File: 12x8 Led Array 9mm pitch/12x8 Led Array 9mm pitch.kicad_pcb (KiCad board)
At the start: 4 copper layers, 189 x 139.9 mm, 313 parts, among them J1 LED ch 1-24, J2 LED ch 25-48, J3 LED ch 49-72, J4 LED ch 73-96, J5 logic/analog, U1 CD74HC4067M96, U2 CD74HC4067M96, U3 CD74HC4067M96, U4 CD74HC4067M96, U5 CD74HC4067M96, U6 CD74HC4067M96

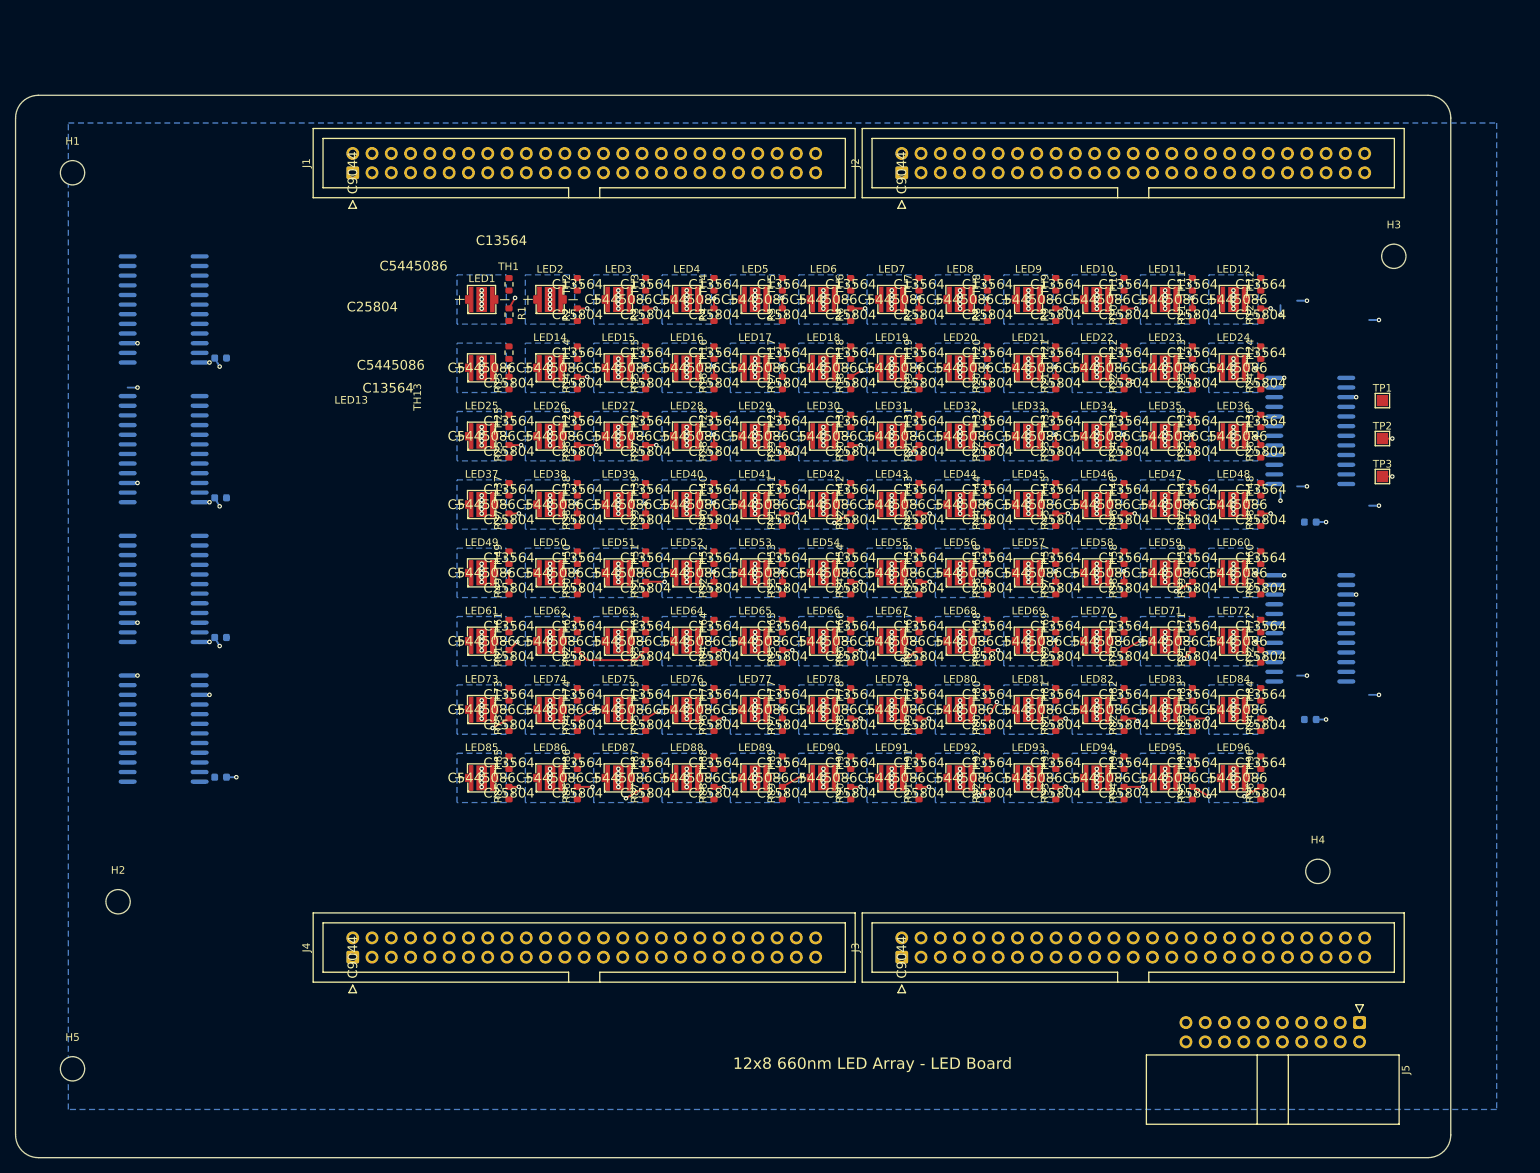
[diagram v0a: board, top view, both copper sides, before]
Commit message: 15mm keep-out from array for all support parts; J5 joins right mux pair
Co-Authored-By: Claude Fable 5 <noreply@anthropic.com>
Claude-Session: https://claude.ai/code/session_017oD54uh7Tvu54u9NPQNcZB
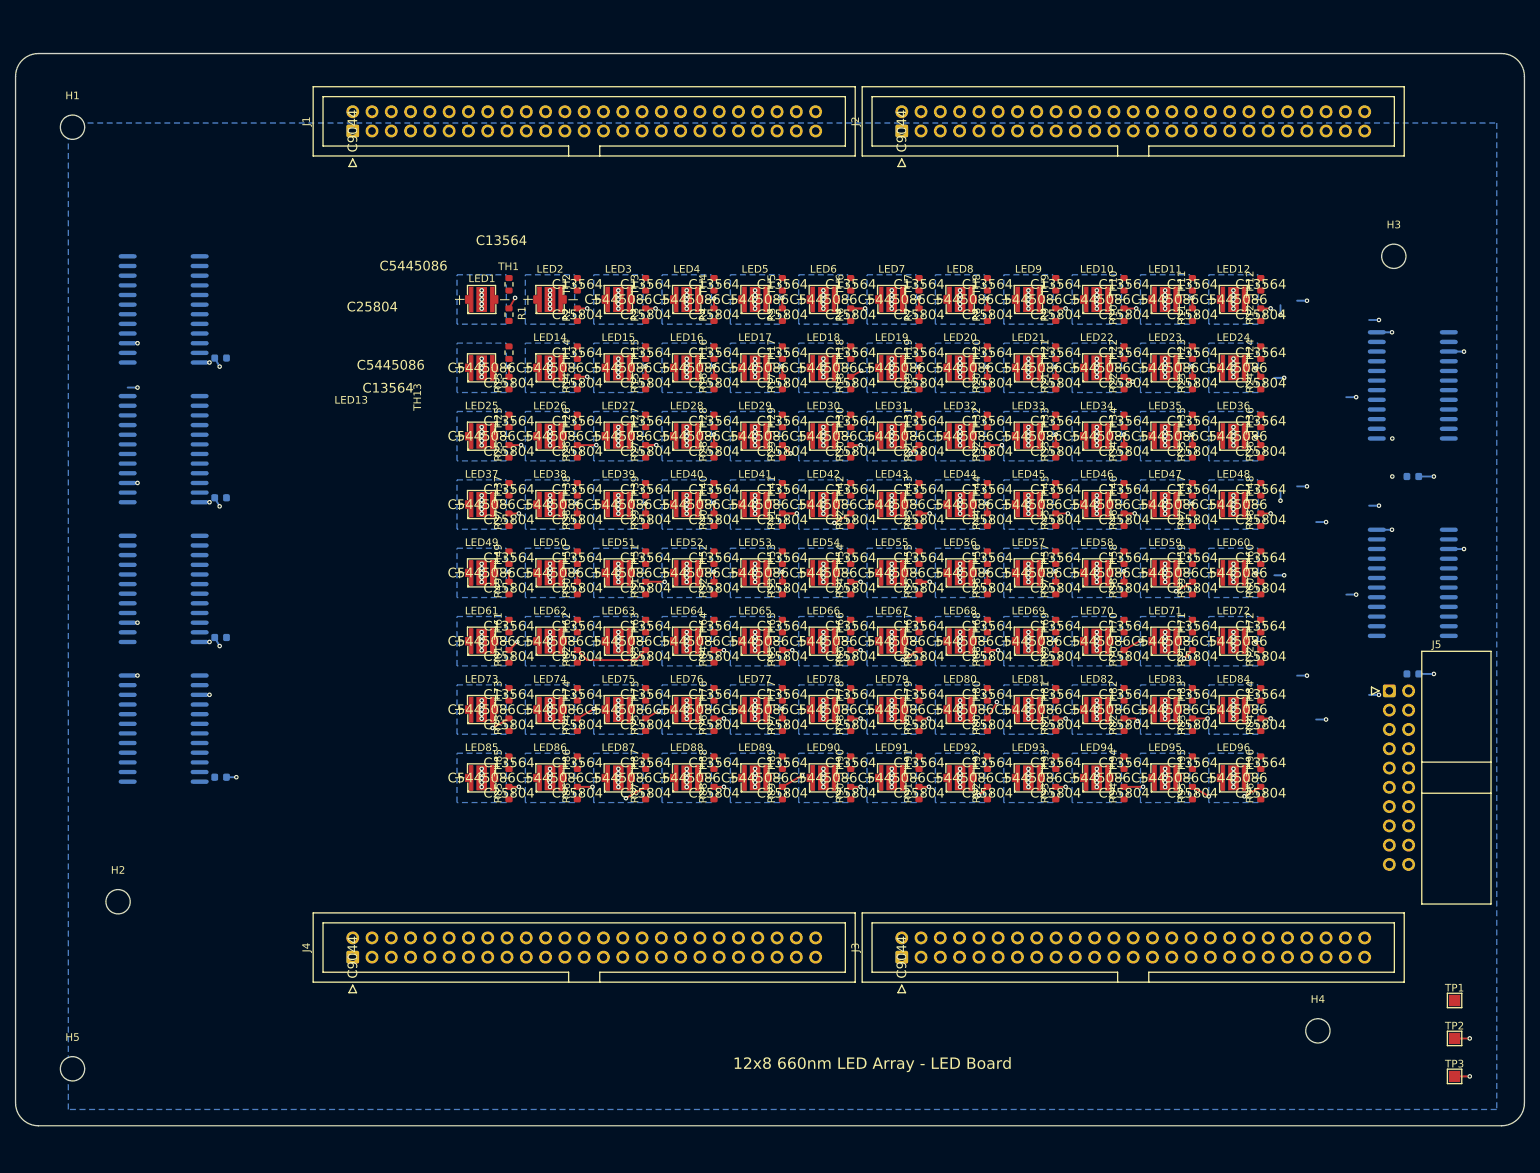
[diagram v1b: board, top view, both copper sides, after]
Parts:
- moved TP1 79.6 mm to (228.0, 141.0)
- moved TP2 79.6 mm to (228.0, 146.0)
- moved TP3 79.6 mm to (228.0, 151.0)
- moved J5 43.9 mm to (219.4, 100.2), turned to 0 degrees
- moved H4 21.0 mm to (210.0, 145.0)
- moved C5 14.8 mm to (222.5, 72.0)
- moved C6 14.8 mm to (222.5, 98.0)
- moved U5 14.8 mm to (222.5, 60.0)
- moved U6 14.8 mm to (222.5, 86.0)
- moved H1 6.00 mm to (46.0, 26.0)
- moved J1 5.50 mm to (82.9, 26.5)
- moved J2 5.50 mm to (155.2, 26.5)
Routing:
- net GND: track 197.0 -> 210.4 mm, vias 123 -> 131
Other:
- board size 189 x 139.9 mm -> 198.7 x 141.2 mm

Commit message: Symmetric aesthetic layout: equal 35mm margins, J5 centered between muxes
- Board 173.7 x 137.7mm, array dead-center both axes
- Left: cap/mux column mirrored by right cap/mux/J5/mux/cap column
- 4 corner holes + bottom-center hole; TP row bottom-right
- Placement DRC clean (cosmetic silk only)

Co-Authored-By: Claude Fable 5 <noreply@anthropic.com>
Claude-Session: https://claude.ai/code/session_017oD54uh7Tvu54u9NPQNcZB
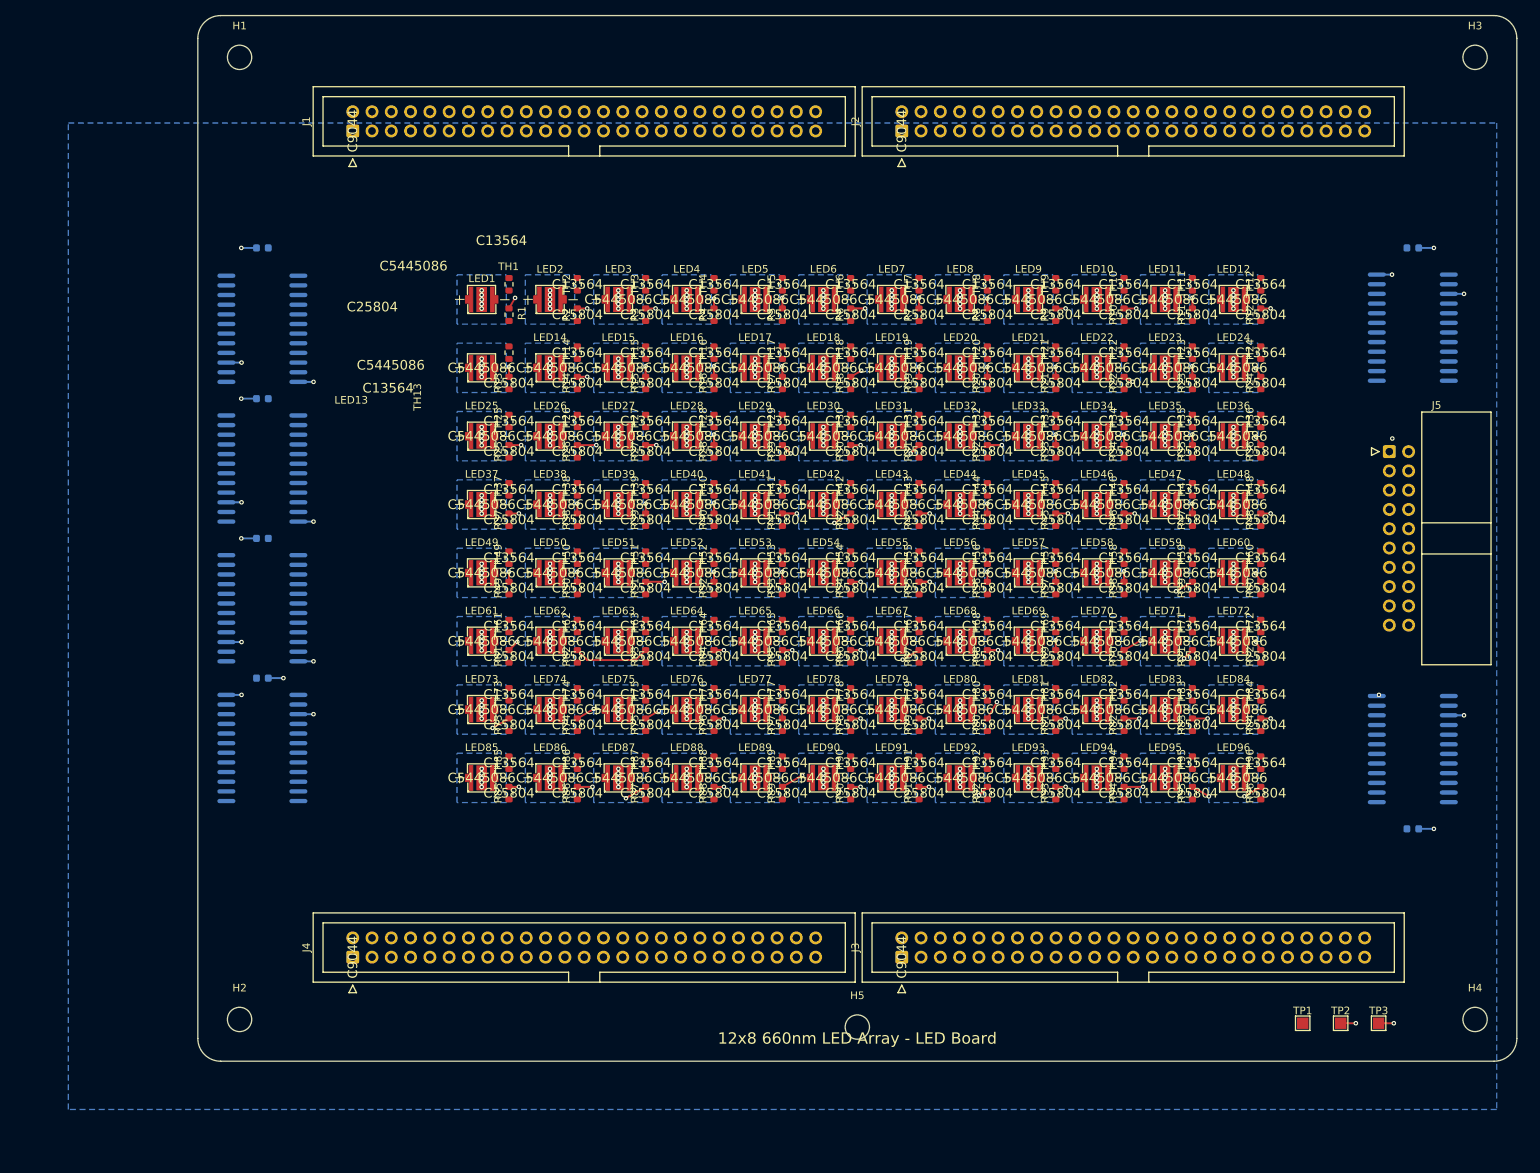
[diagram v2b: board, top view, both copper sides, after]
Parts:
- moved H5 103.5 mm to (149.3, 144.5)
- moved J5 31.5 mm to (219.4, 68.7)
- moved C5 30.1 mm to (222.5, 41.9)
- moved H3 28.3 mm to (230.7, 16.8)
- moved H1 23.8 mm to (68.0, 16.8)
- moved H2 22.3 mm to (68.0, 143.5)
- moved U6 21.9 mm to (222.5, 107.9)
- moved H4 20.8 mm to (230.7, 143.5)
- moved C6 20.4 mm to (222.5, 118.4)
- moved TP1 20.2 mm to (208.0, 144.0)
- moved C1 15.5 mm to (71.0, 41.9)
- moved TP2 15.1 mm to (213.0, 144.0)
- moved C2 14.2 mm to (71.0, 61.8)
- moved C3 14.2 mm to (71.0, 80.2)
- moved C4 14.2 mm to (71.0, 98.5)
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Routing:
- net GND: track 210.4 -> 198.7 mm, vias 131 -> 115
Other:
- board size 198.7 x 141.2 mm -> 173.7 x 137.7 mm
